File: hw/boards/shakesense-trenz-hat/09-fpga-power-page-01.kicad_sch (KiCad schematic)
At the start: 6 parts

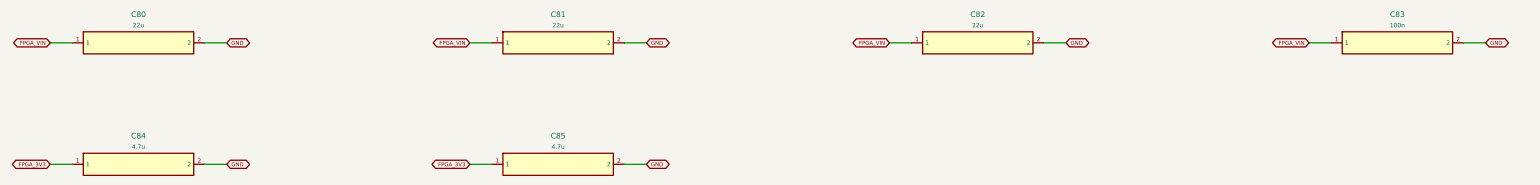
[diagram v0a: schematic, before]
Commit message: Expose Trenz GPIOs on the Pi-outline HDI sensor HAT
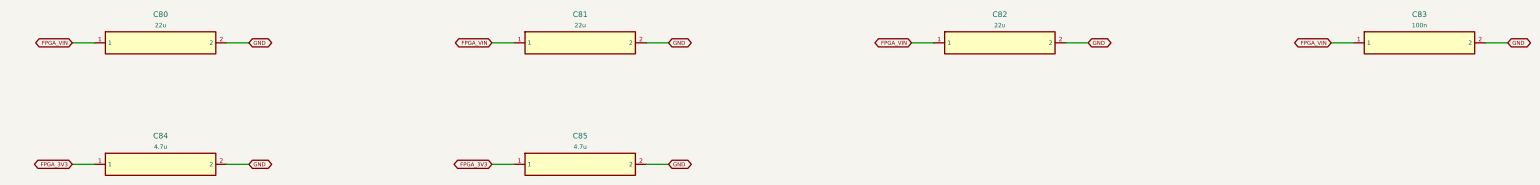
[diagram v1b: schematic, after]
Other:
- title: shakesense-trenz-hat / 09-fpga-power-page-01 -> ShakeSense T1 / 09-fpga-power-page-01
- moved on the sheet: C80, C81, C82, C83, C84, C85
